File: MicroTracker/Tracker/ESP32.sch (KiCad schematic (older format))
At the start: 13 parts, among them U6 ESP32-WROOM-32D

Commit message: added connections
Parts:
- added R? (x2): 10k, Resistor_SMD:R_0805_2012Metric_Pad1.15x1.40mm_HandSolder, symbol Device:R
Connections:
- net +3V3: now also R?.1, R?.1
- net SCK: now also R?.2
- net SDA: now also R?.2
- net Transceiver_RX: now also U6.27 (IO16)
- net Transceiver_TX: now also U6.28 (IO17)
- net v_bat_measure: now also U6.16 (IO13)
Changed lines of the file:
@@
 Text HLabel 6300 3000 2    50   Input ~ 0
 v_bat_measure
-Text HLabel 7350 3150 0    50   Input ~ 0
+Text HLabel 6300 3300 2    50   Input ~ 0
 Transceiver_RX
-Text HLabel 7350 3250 0    50   Input ~ 0
+Text HLabel 6300 3400 2    50   Input ~ 0
 Transceiver_TX
-Text HLabel 7350 3450 0    50   Input ~ 0
+Text HLabel 6300 4300 2    50   Input ~ 0
 GPS_RX
-Text HLabel 7350 3550 0    50   Input ~ 0
+Text HLabel 6300 4400 2    50   Input ~ 0
 GPS_TX
 Wire Wire Line
@@
 En
 Wire Wire Line
-	6200 3800 6300 3800
-Wire Wire Line
 	6200 2300 6300 2300
-Text HLabel 6300 3700 2    50   Input ~ 0
+Text HLabel 8900 3700 2    50   Input ~ 0
 SDA
-Text HLabel 6300 3800 2    50   Input ~ 0
+Text HLabel 8900 3800 2    50   Input ~ 0
 SCK
-Wire Wire Line
-	6200 3700 6300 3700
 NoConn ~ 5000 2500
 NoConn ~ 5000 2600
@@
 Wire Notes Line
 	4400 5400 550  5400
+Wire Wire Line
+	6200 3700 7900 3700
+Wire Wire Line
+	6200 3800 8300 3800
+$Comp
+L power:+3.3V #PWR?
+U 1 1 5F0B76DD
+P 7900 3150
+AR Path="/5EF7F2B3/5F0B76DD" Ref="#PWR?"  Part="1"
+AR Path="/5EF7F634/5F0B76DD" Ref="#PWR?"  Part="1"
+F 0 "#PWR?" H 7900 3000 50  0001 C CNN
+F 1 "+3.3V" H 7915 3323 50  0000 C CNN
+F 2 "" H 7900 3150 50  0001 C CNN
+F 3 "" H 7900 3150 50  0001 C CNN
+	1    7900 3150
+	1    0    0    -1
+$EndComp
+$Comp
+L power:+3.3V #PWR?
+U 1 1 5F0B76E3
+P 8300 3150
+AR Path="/5EF7F2B3/5F0B76E3" Ref="#PWR?"  Part="1"
+AR Path="/5EF7F634/5F0B76E3" Ref="#PWR?"  Part="1"
+F 0 "#PWR?" H 8300 3000 50  0001 C CNN
+F 1 "+3.3V" H 8315 3323 50  0000 C CNN
+F 2 "" H 8300 3150 50  0001 C CNN
+F 3 "" H 8300 3150 50  0001 C CNN
+	1    8300 3150
+	1    0    0    -1
+$EndComp
+Wire Wire Line
+	7900 3150 7900 3250
+Wire Wire Line
+	8300 3150 8300 3250
+$Comp
+L Device:R R?
+U 1 1 5F0B76EB
+P 7900 3400
+AR Path="/5EF7F2B3/5F0B76EB" Ref="R?"  Part="1"
+AR Path="/5EF7F634/5F0B76EB" Ref="R?"  Part="1"
+F 0 "R?" H 7970 3446 50  0000 L CNN
+F 1 "10k" H 7970 3355 50  0000 L CNN
+F 2 "Resistor_SMD:R_0805_2012Metric_Pad1.15x1.40mm_HandSolder" V 7830 3400 50  0001 C CNN
+F 3 "~" H 7900 3400 50  0001 C CNN
+	1    7900 3400
+	1    0    0    -1
+$EndComp
+$Comp
+L Device:R R?
+U 1 1 5F0B76F1
+P 8300 3400
+AR Path="/5EF7F2B3/5F0B76F1" Ref="R?"  Part="1"
+AR Path="/5EF7F634/5F0B76F1" Ref="R?"  Part="1"
+F 0 "R?" H 8370 3446 50  0000 L CNN
+F 1 "10k" H 8370 3355 50  0000 L CNN
+F 2 "Resistor_SMD:R_0805_2012Metric_Pad1.15x1.40mm_HandSolder" V 8230 3400 50  0001 C CNN
+F 3 "~" H 8300 3400 50  0001 C CNN
+	1    8300 3400
+	1    0    0    -1
+$EndComp
+Wire Wire Line
+	7900 3550 7900 3700
+Connection ~ 7900 3700
+Wire Wire Line
+	7900 3700 8900 3700
+Wire Wire Line
+	8300 3550 8300 3800
+Connection ~ 8300 3800
+Wire Wire Line
+	8300 3800 8900 3800
+Wire Wire Line
+	6200 3400 6300 3400
+Wire Wire Line
+	6200 3300 6300 3300
+Wire Wire Line
+	6200 3000 6300 3000
 $EndSCHEMATC

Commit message: started working on gps
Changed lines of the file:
@@
 Text HLabel 6300 4400 2    50   Input ~ 0
 GPS_TX
-Wire Wire Line
-	6200 4100 6350 4100
 Text GLabel 1500 6350 2    50   Input ~ 0
 En
@@
 Wire Wire Line
 	6200 3000 6300 3000
+Text HLabel 6300 4600 2    50   Input ~ 0
+charge1Trigger
+Text HLabel 6300 4500 2    50   Input ~ 0
+charge2Trigger
+Text HLabel 6300 4100 2    50   Input ~ 0
+charge2Sense
+Text HLabel 6300 4200 2    50   Input ~ 0
+charge1Sense
 $EndSCHEMATC

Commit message: added charges
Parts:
- gave numbers to parts that had none: 14
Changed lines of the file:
@@
 En
 $Comp
-L power:+3.3V #PWR?
+L power:+3.3V #PWR0148
 U 1 1 5F03E4F6
 P 1300 5850
-F 0 "#PWR?" H 1300 5700 50  0001 C CNN
+F 0 "#PWR0148" H 1300 5700 50  0001 C CNN
 F 1 "+3.3V" H 1315 6023 50  0000 C CNN
 F 2 "" H 1300 5850 50  0001 C CNN
@@
 $EndComp
 $Comp
-L power:GND #PWR?
+L power:GND #PWR0149
 U 1 1 5F03EC46
 P 1300 7300
-F 0 "#PWR?" H 1300 7050 50  0001 C CNN
+F 0 "#PWR0149" H 1300 7050 50  0001 C CNN
 F 1 "GND" H 1305 7127 50  0000 C CNN
 F 2 "" H 1300 7300 50  0001 C CNN
@@
 $EndComp
 $Comp
-L Device:C C?
+L Device:C C13
 U 1 1 5F03F2A2
 P 900 6600
-F 0 "C?" H 1015 6646 50  0000 L CNN
+F 0 "C13" H 1015 6646 50  0000 L CNN
 F 1 "0.1uF" H 1015 6555 50  0000 L CNN
 F 2 "" H 938 6450 50  0001 C CNN
@@
 $EndComp
 $Comp
-L Device:R R?
+L Device:R R11
 U 1 1 5F03FA29
 P 1300 6100
-F 0 "R?" H 1370 6146 50  0000 L CNN
+F 0 "R11" H 1370 6146 50  0000 L CNN
 F 1 "12k" H 1370 6055 50  0000 L CNN
 F 2 "" V 1230 6100 50  0001 C CNN
@@
 $EndComp
 $Comp
-L Device:R R?
+L Device:R R12
 U 1 1 5F040398
 P 1300 6550
-F 0 "R?" H 1370 6596 50  0000 L CNN
+F 0 "R12" H 1370 6596 50  0000 L CNN
 F 1 "470" H 1370 6505 50  0000 L CNN
 F 2 "" V 1230 6550 50  0001 C CNN
@@
 $EndComp
 $Comp
-L Switch:SW_Push SW?
+L Switch:SW_Push SW2
 U 1 1 5F040E7E
 P 1300 7000
-F 0 "SW?" V 1254 7148 50  0000 L CNN
+F 0 "SW2" V 1254 7148 50  0000 L CNN
 F 1 "SW_Push" V 1345 7148 50  0000 L CNN
 F 2 "" H 1300 7200 50  0001 C CNN
@@
 Flash
 $Comp
-L power:+3.3V #PWR?
+L power:+3.3V #PWR0150
 U 1 1 5F04C489
 P 2350 5850
-F 0 "#PWR?" H 2350 5700 50  0001 C CNN
+F 0 "#PWR0150" H 2350 5700 50  0001 C CNN
 F 1 "+3.3V" H 2365 6023 50  0000 C CNN
 F 2 "" H 2350 5850 50  0001 C CNN
@@
 $EndComp
 $Comp
-L power:GND #PWR?
+L power:GND #PWR0151
 U 1 1 5F04C48F
 P 2350 7300
-F 0 "#PWR?" H 2350 7050 50  0001 C CNN
+F 0 "#PWR0151" H 2350 7050 50  0001 C CNN
 F 1 "GND" H 2355 7127 50  0000 C CNN
 F 2 "" H 2350 7300 50  0001 C CNN
@@
 $EndComp
 $Comp
-L Device:C C?
+L Device:C C14
 U 1 1 5F04C495
 P 1950 6600
-F 0 "C?" H 2065 6646 50  0000 L CNN
+F 0 "C14" H 2065 6646 50  0000 L CNN
 F 1 "0.1uF" H 2065 6555 50  0000 L CNN
 F 2 "" H 1988 6450 50  0001 C CNN
@@
 $EndComp
 $Comp
-L Device:R R?
+L Device:R R13
 U 1 1 5F04C49B
 P 2350 6100
-F 0 "R?" H 2420 6146 50  0000 L CNN
+F 0 "R13" H 2420 6146 50  0000 L CNN
 F 1 "12k" H 2420 6055 50  0000 L CNN
 F 2 "" V 2280 6100 50  0001 C CNN
@@
 $EndComp
 $Comp
-L Device:R R?
+L Device:R R14
 U 1 1 5F04C4A1
 P 2350 6550
-F 0 "R?" H 2420 6596 50  0000 L CNN
+F 0 "R14" H 2420 6596 50  0000 L CNN
 F 1 "470" H 2420 6505 50  0000 L CNN
 F 2 "" V 2280 6550 50  0001 C CNN
@@
 $EndComp
 $Comp
-L Switch:SW_Push SW?
+L Switch:SW_Push SW3
 U 1 1 5F04C4A7
 P 2350 7000
-F 0 "SW?" V 2304 7148 50  0000 L CNN
+F 0 "SW3" V 2304 7148 50  0000 L CNN
 F 1 "SW_Push" V 2395 7148 50  0000 L CNN
 F 2 "" H 2350 7200 50  0001 C CNN
@@
 	2550 6350 2350 6350
 $Comp
-L power:GND #PWR?
+L power:GND #PWR0152
 U 1 1 5F04C95F
 P 3400 7300
-F 0 "#PWR?" H 3400 7050 50  0001 C CNN
+F 0 "#PWR0152" H 3400 7050 50  0001 C CNN
 F 1 "GND" H 3405 7127 50  0000 C CNN
 F 2 "" H 3400 7300 50  0001 C CNN
@@
 $EndComp
 $Comp
-L Device:LED D?
+L Device:LED D4
 U 1 1 5F04CFA0
 P 3400 6600
-F 0 "D?" V 3439 6483 50  0000 R CNN
+F 0 "D4" V 3439 6483 50  0000 R CNN
 F 1 "LED" V 3348 6483 50  0000 R CNN
 F 2 "" H 3400 6600 50  0001 C CNN
@@
 $EndComp
 $Comp
-L Device:R R?
+L Device:R R15
 U 1 1 5F04E44C
 P 3400 7050
-F 0 "R?" H 3470 7096 50  0000 L CNN
+F 0 "R15" H 3470 7096 50  0000 L CNN
 F 1 "220" H 3470 7005 50  0000 L CNN
 F 2 "" V 3330 7050 50  0001 C CNN
@@
 	6200 3200 6250 3200
 $Comp
-L Device:C C?
+L Device:C C15
 U 1 1 5F074C42
 P 6500 1500
-F 0 "C?" H 6615 1546 50  0000 L CNN
+F 0 "C15" H 6615 1546 50  0000 L CNN
 F 1 "10uF" H 6615 1455 50  0000 L CNN
 F 2 "" H 6538 1350 50  0001 C CNN
@@
 $EndComp
 $Comp
-L Device:C C?
+L Device:C C16
 U 1 1 5F075251
 P 6900 1500
-F 0 "C?" H 7015 1546 50  0000 L CNN
+F 0 "C16" H 7015 1546 50  0000 L CNN
 F 1 "0.1uF" H 7015 1455 50  0000 L CNN
 F 2 "" H 6938 1350 50  0001 C CNN
@@
 $EndComp
 $Comp
-L power:GND #PWR?
+L power:GND #PWR0153
 U 1 1 5F0759ED
 P 6700 1800
-F 0 "#PWR?" H 6700 1550 50  0001 C CNN
+F 0 "#PWR0153" H 6700 1550 50  0001 C CNN
 F 1 "GND" H 6705 1627 50  0000 C CNN
 F 2 "" H 6700 1800 50  0001 C CNN
@@
 P 7900 3150
 AR Path="/5EF7F2B3/5F0B76DD" Ref="#PWR?"  Part="1"
-AR Path="/5EF7F634/5F0B76DD" Ref="#PWR?"  Part="1"
-F 0 "#PWR?" H 7900 3000 50  0001 C CNN
+AR Path="/5EF7F634/5F0B76DD" Ref="#PWR0154"  Part="1"
+F 0 "#PWR0154" H 7900 3000 50  0001 C CNN
 F 1 "+3.3V" H 7915 3323 50  0000 C CNN
 F 2 "" H 7900 3150 50  0001 C CNN
@@
 P 8300 3150
 AR Path="/5EF7F2B3/5F0B76E3" Ref="#PWR?"  Part="1"
-AR Path="/5EF7F634/5F0B76E3" Ref="#PWR?"  Part="1"
-F 0 "#PWR?" H 8300 3000 50  0001 C CNN
+AR Path="/5EF7F634/5F0B76E3" Ref="#PWR0155"  Part="1"
+F 0 "#PWR0155" H 8300 3000 50  0001 C CNN
 F 1 "+3.3V" H 8315 3323 50  0000 C CNN
 F 2 "" H 8300 3150 50  0001 C CNN
@@
 P 7900 3400
 AR Path="/5EF7F2B3/5F0B76EB" Ref="R?"  Part="1"
-AR Path="/5EF7F634/5F0B76EB" Ref="R?"  Part="1"
-F 0 "R?" H 7970 3446 50  0000 L CNN
+AR Path="/5EF7F634/5F0B76EB" Ref="R16"  Part="1"
+F 0 "R16" H 7970 3446 50  0000 L CNN
 F 1 "10k" H 7970 3355 50  0000 L CNN
 F 2 "Resistor_SMD:R_0805_2012Metric_Pad1.15x1.40mm_HandSolder" V 7830 3400 50  0001 C CNN
@@
 P 8300 3400
 AR Path="/5EF7F2B3/5F0B76F1" Ref="R?"  Part="1"
-AR Path="/5EF7F634/5F0B76F1" Ref="R?"  Part="1"
-F 0 "R?" H 8370 3446 50  0000 L CNN
+AR Path="/5EF7F634/5F0B76F1" Ref="R17"  Part="1"
+F 0 "R17" H 8370 3446 50  0000 L CNN
 F 1 "10k" H 8370 3355 50  0000 L CNN
 F 2 "Resistor_SMD:R_0805_2012Metric_Pad1.15x1.40mm_HandSolder" V 8230 3400 50  0001 C CNN

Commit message: assigned parts
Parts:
- C13, C14, C15, C16: footprint (none) -> Capacitor_SMD:C_0805_2012Metric_Pad1.15x1.40mm_HandSolder
- D4: footprint (none) -> LED_SMD:LED_0805_2012Metric_Pad1.15x1.40mm_HandSolder
- R11, R12, R13, R14, R15: footprint (none) -> Resistor_SMD:R_0805_2012Metric_Pad1.15x1.40mm_HandSolder
- SW2, SW3: footprint (none) -> Sparkfun-Artemis:SW_TL1015AF160QG
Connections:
- net GPS_RX: now also U6.17 (SHD/SD2)
- net GPS_TX: now also U6.18 (SWP/SD3)
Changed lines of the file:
@@
 Text HLabel 6300 3400 2    50   Input ~ 0
 Transceiver_TX
-Text HLabel 6300 4300 2    50   Input ~ 0
+Text HLabel 4850 3700 0    50   Input ~ 0
 GPS_RX
-Text HLabel 6300 4400 2    50   Input ~ 0
+Text HLabel 4850 3800 0    50   Input ~ 0
 GPS_TX
 Text GLabel 1500 6350 2    50   Input ~ 0
@@
 F 0 "C13" H 1015 6646 50  0000 L CNN
 F 1 "0.1uF" H 1015 6555 50  0000 L CNN
-F 2 "" H 938 6450 50  0001 C CNN
+F 2 "Capacitor_SMD:C_0805_2012Metric_Pad1.15x1.40mm_HandSolder" H 938 6450 50  0001 C CNN
 F 3 "~" H 900 6600 50  0001 C CNN
 	1    900  6600
@@
 F 0 "R11" H 1370 6146 50  0000 L CNN
 F 1 "12k" H 1370 6055 50  0000 L CNN
-F 2 "" V 1230 6100 50  0001 C CNN
+F 2 "Resistor_SMD:R_0805_2012Metric_Pad1.15x1.40mm_HandSolder" V 1230 6100 50  0001 C CNN
 F 3 "~" H 1300 6100 50  0001 C CNN
 	1    1300 6100
@@
 F 0 "R12" H 1370 6596 50  0000 L CNN
 F 1 "470" H 1370 6505 50  0000 L CNN
-F 2 "" V 1230 6550 50  0001 C CNN
+F 2 "Resistor_SMD:R_0805_2012Metric_Pad1.15x1.40mm_HandSolder" V 1230 6550 50  0001 C CNN
 F 3 "~" H 1300 6550 50  0001 C CNN
 	1    1300 6550
@@
 F 0 "SW2" V 1254 7148 50  0000 L CNN
 F 1 "SW_Push" V 1345 7148 50  0000 L CNN
-F 2 "" H 1300 7200 50  0001 C CNN
+F 2 "Sparkfun-Artemis:SW_TL1015AF160QG" H 1300 7200 50  0001 C CNN
 F 3 "~" H 1300 7200 50  0001 C CNN
 	1    1300 7000
@@
 F 0 "C14" H 2065 6646 50  0000 L CNN
 F 1 "0.1uF" H 2065 6555 50  0000 L CNN
-F 2 "" H 1988 6450 50  0001 C CNN
+F 2 "Capacitor_SMD:C_0805_2012Metric_Pad1.15x1.40mm_HandSolder" H 1988 6450 50  0001 C CNN
 F 3 "~" H 1950 6600 50  0001 C CNN
 	1    1950 6600
@@
 F 0 "R13" H 2420 6146 50  0000 L CNN
 F 1 "12k" H 2420 6055 50  0000 L CNN
-F 2 "" V 2280 6100 50  0001 C CNN
+F 2 "Resistor_SMD:R_0805_2012Metric_Pad1.15x1.40mm_HandSolder" V 2280 6100 50  0001 C CNN
 F 3 "~" H 2350 6100 50  0001 C CNN
 	1    2350 6100
@@
 F 0 "R14" H 2420 6596 50  0000 L CNN
 F 1 "470" H 2420 6505 50  0000 L CNN
-F 2 "" V 2280 6550 50  0001 C CNN
+F 2 "Resistor_SMD:R_0805_2012Metric_Pad1.15x1.40mm_HandSolder" V 2280 6550 50  0001 C CNN
 F 3 "~" H 2350 6550 50  0001 C CNN
 	1    2350 6550
@@
 F 0 "SW3" V 2304 7148 50  0000 L CNN
 F 1 "SW_Push" V 2395 7148 50  0000 L CNN
-F 2 "" H 2350 7200 50  0001 C CNN
+F 2 "Sparkfun-Artemis:SW_TL1015AF160QG" H 2350 7200 50  0001 C CNN
 F 3 "~" H 2350 7200 50  0001 C CNN
 	1    2350 7000
@@
 F 0 "D4" V 3439 6483 50  0000 R CNN
 F 1 "LED" V 3348 6483 50  0000 R CNN
-F 2 "" H 3400 6600 50  0001 C CNN
+F 2 "LED_SMD:LED_0805_2012Metric_Pad1.15x1.40mm_HandSolder" H 3400 6600 50  0001 C CNN
 F 3 "~" H 3400 6600 50  0001 C CNN
 	1    3400 6600
@@
 F 0 "R15" H 3470 7096 50  0000 L CNN
 F 1 "220" H 3470 7005 50  0000 L CNN
-F 2 "" V 3330 7050 50  0001 C CNN
+F 2 "Resistor_SMD:R_0805_2012Metric_Pad1.15x1.40mm_HandSolder" V 3330 7050 50  0001 C CNN
 F 3 "~" H 3400 7050 50  0001 C CNN
 	1    3400 7050
@@
 F 0 "C15" H 6615 1546 50  0000 L CNN
 F 1 "10uF" H 6615 1455 50  0000 L CNN
-F 2 "" H 6538 1350 50  0001 C CNN
+F 2 "Capacitor_SMD:C_0805_2012Metric_Pad1.15x1.40mm_HandSolder" H 6538 1350 50  0001 C CNN
 F 3 "~" H 6500 1500 50  0001 C CNN
 	1    6500 1500
@@
 F 0 "C16" H 7015 1546 50  0000 L CNN
 F 1 "0.1uF" H 7015 1455 50  0000 L CNN
-F 2 "" H 6938 1350 50  0001 C CNN
+F 2 "Capacitor_SMD:C_0805_2012Metric_Pad1.15x1.40mm_HandSolder" H 6938 1350 50  0001 C CNN
 F 3 "~" H 6900 1500 50  0001 C CNN
 	1    6900 1500
@@
 Text HLabel 6300 4200 2    50   Input ~ 0
 charge1Sense
+Wire Wire Line
+	4850 3700 5000 3700
+Wire Wire Line
+	4850 3800 5000 3800
 $EndSCHEMATC

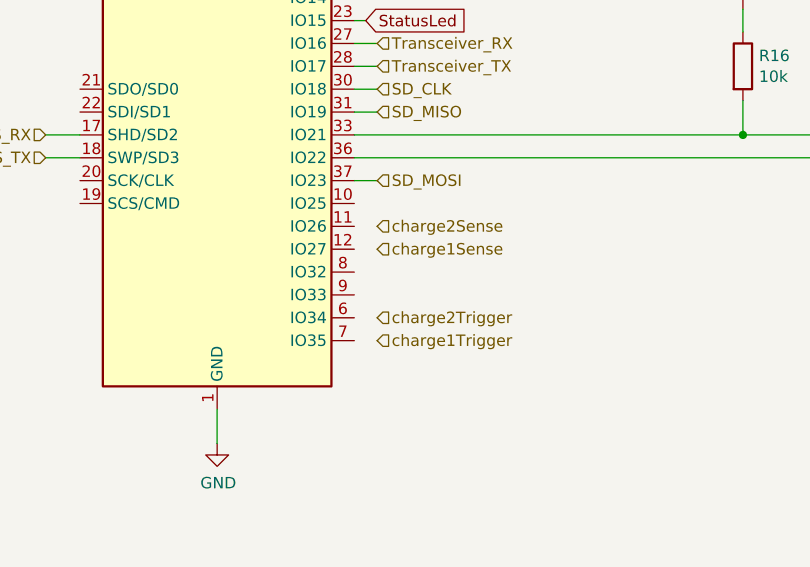
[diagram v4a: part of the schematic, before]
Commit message: added more parts and lib
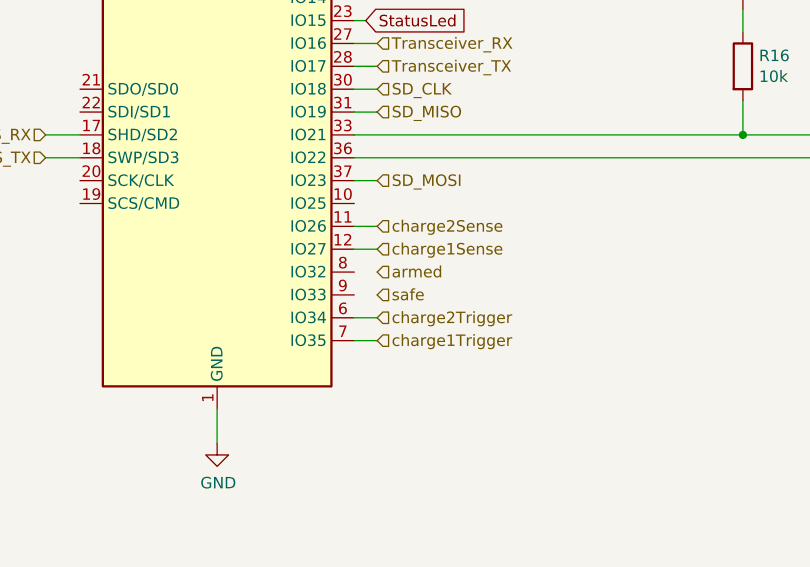
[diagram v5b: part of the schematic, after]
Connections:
- net charge1Sense: now also U6.12 (IO27)
- net charge1Trigger: now also U6.7 (IO35)
- net charge2Sense: now also U6.11 (IO26)
- net charge2Trigger: now also U6.6 (IO34)
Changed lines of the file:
@@
 Wire Wire Line
 	4850 3800 5000 3800
+Wire Wire Line
+	6200 4100 6300 4100
+Wire Wire Line
+	6200 4200 6300 4200
+Wire Wire Line
+	6200 4500 6300 4500
+Wire Wire Line
+	6200 4600 6300 4600
+Text HLabel 6300 4300 2    50   Input ~ 0
+armed
+Text HLabel 6300 4400 2    50   Input ~ 0
+safe
 $EndSCHEMATC

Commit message: fixed errors
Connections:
- no-connect marks 2 -> 13
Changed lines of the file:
@@
 Text HLabel 6300 4400 2    50   Input ~ 0
 safe
+NoConn ~ 5000 3500
+NoConn ~ 5000 3600
+NoConn ~ 5000 3900
+NoConn ~ 5000 4000
+NoConn ~ 6200 2500
+NoConn ~ 6200 2700
+NoConn ~ 6200 2900
+NoConn ~ 6200 3100
+NoConn ~ 6200 4000
+NoConn ~ 6200 4300
+NoConn ~ 6200 4400
 $EndSCHEMATC
